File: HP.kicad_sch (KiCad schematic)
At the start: 4 parts, among them U1 BTS50010-1TAD-TBD, U2 BTS50010-1TAD-TBD, U3 BTS50010-1TAD-TBD, U4 BTS50010-1TAD-TBD

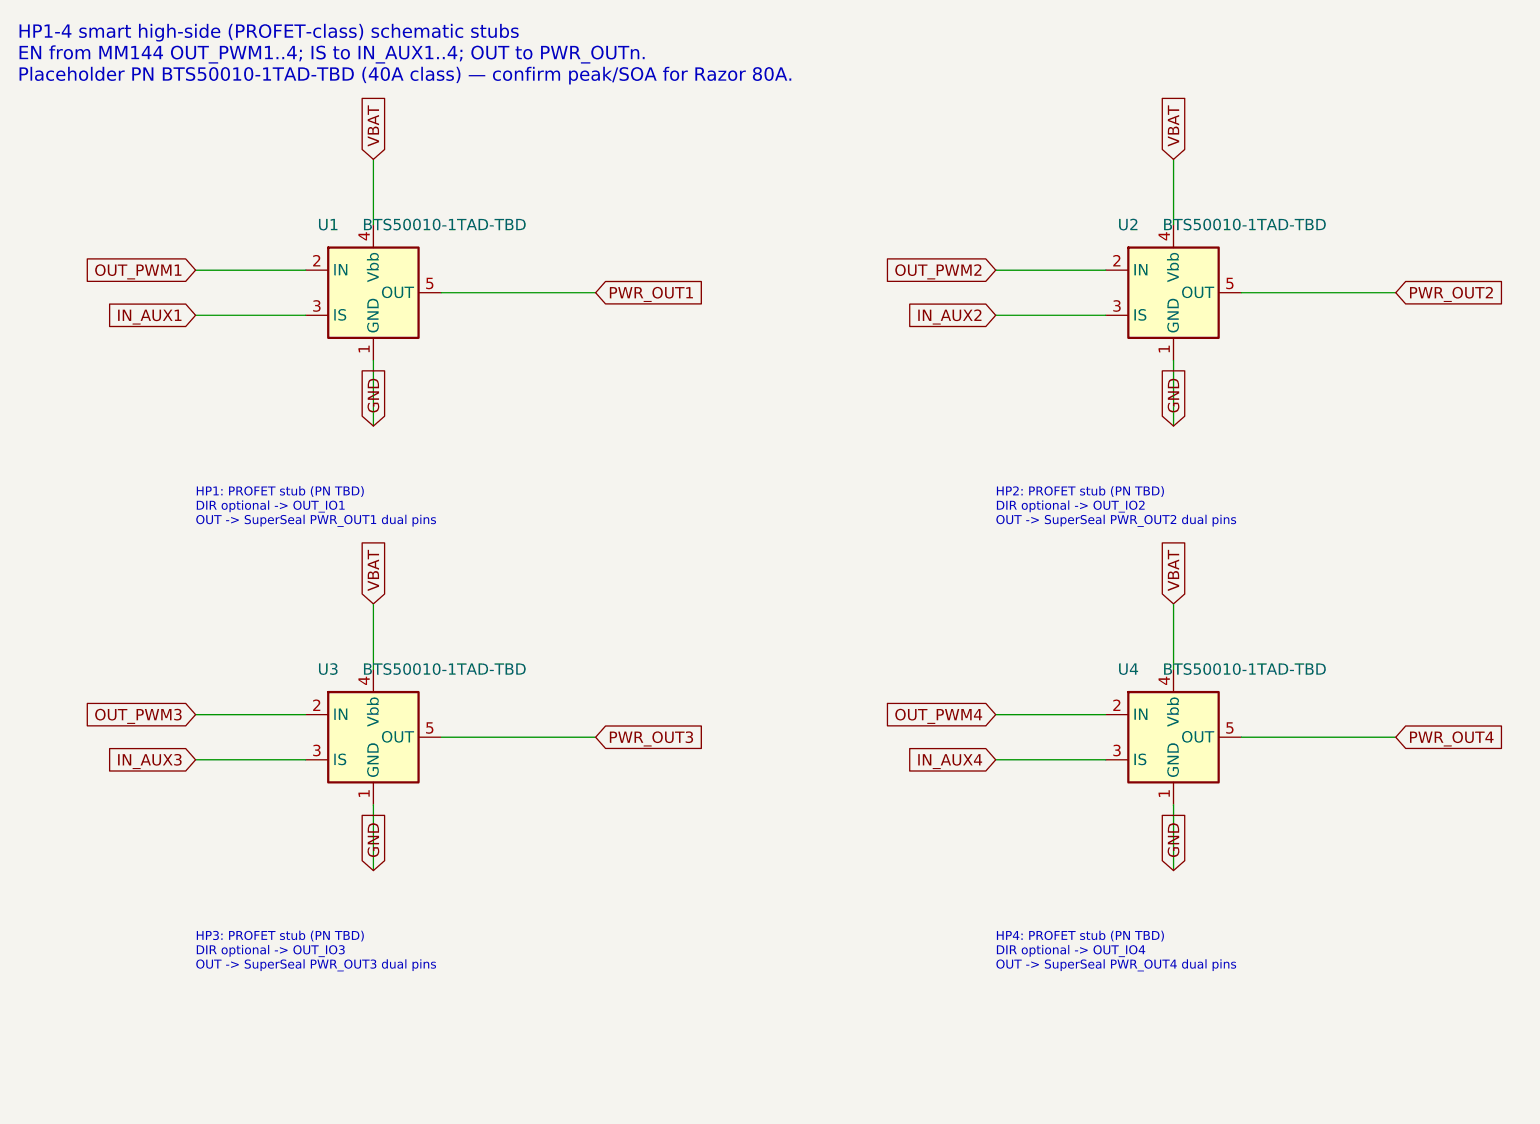
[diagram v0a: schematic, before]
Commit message: Clear fab blockers 1–4: SuperSeal 9-6437287-8, PROFET PNs, power entry, PCB place
- Replace Conn_02x13 pin-header with TE/AMP SuperSeal 1.0 26-way
  (9-6437287-8, keying 1) via pdmrazora.pretty footprint (6473423-1 pattern)
- HP: keep BTS50010-1TAD; add RIS 2k7 + 10n; fix IN/IS wiring
- ADIO: BTS7004-1EPP; RIS 4k7 + soft PU 4k7 to SENSOR_5V; fix EN/IS wiring
- Power entry: fuse/TVS/bulk stubs + IGN_SW 100k/10k (~11:1) → IN_VIGN
- PCB: place SuperSeal, HP×4, ADIO×8 with nets; outline 180×140; thermal zones
- Document PNs, kILIS, AmpsPerVolt TODOs in HARDWARE_BOM.md / BOARD.md

Do not touch HELLCORE.
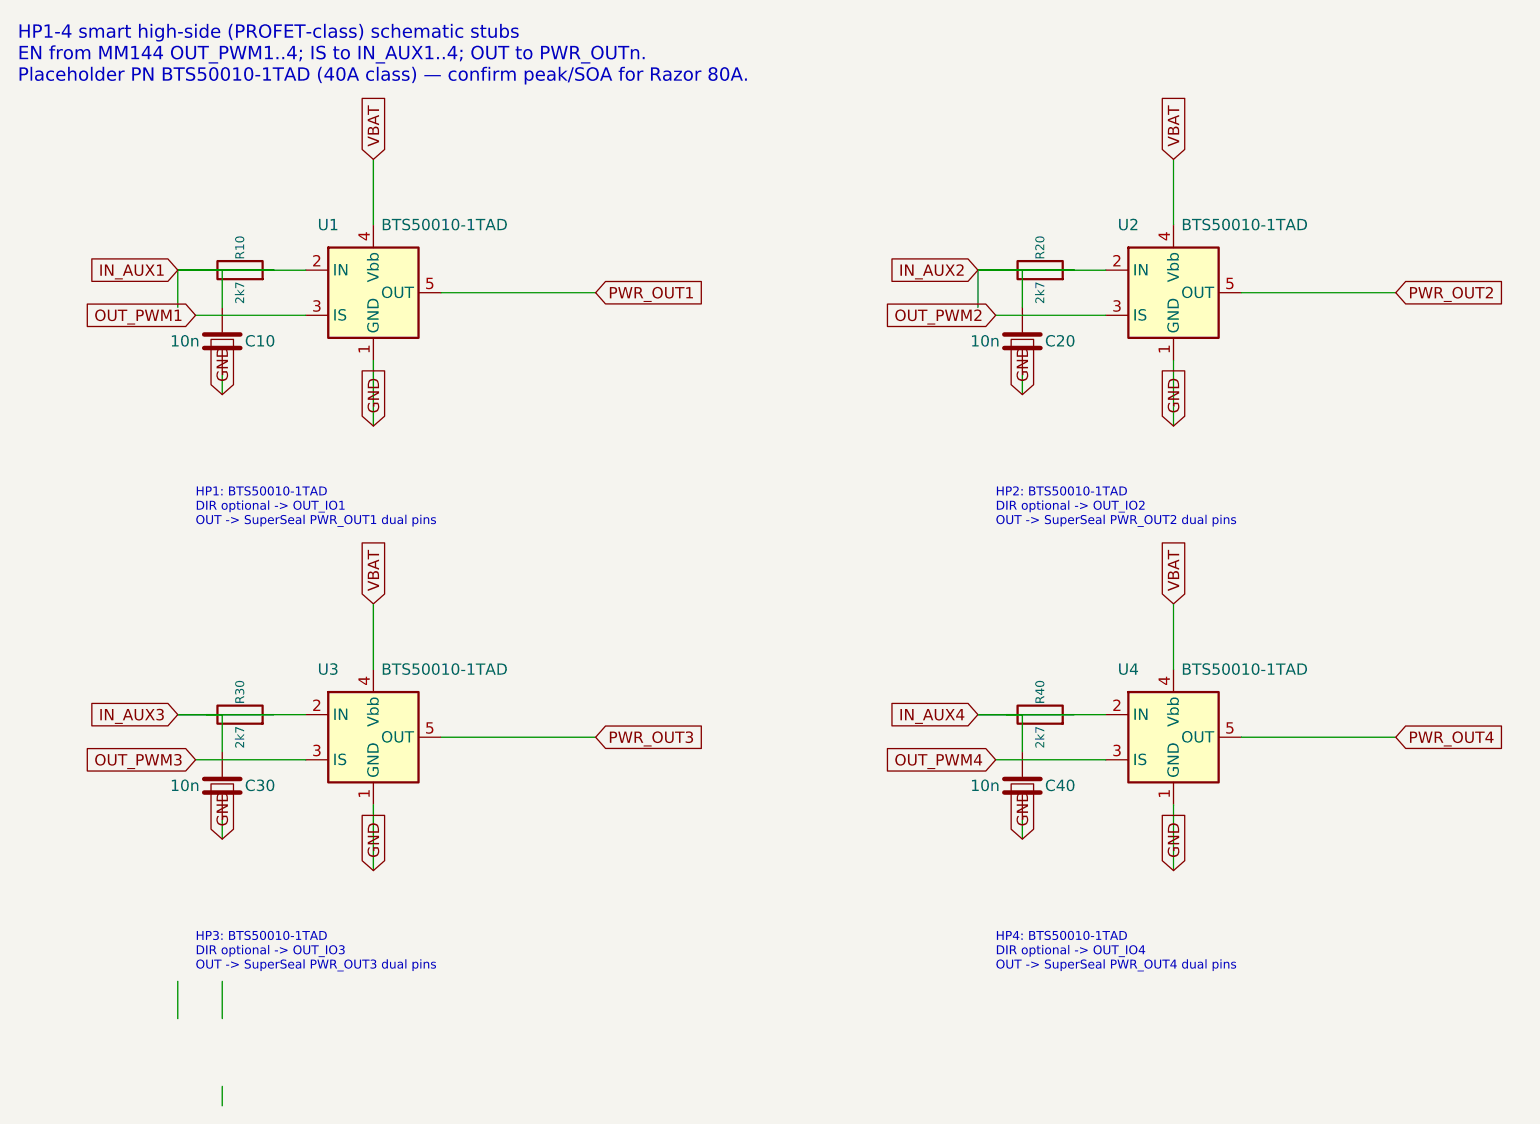
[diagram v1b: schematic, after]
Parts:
- added C10, C20, C30, C40: 10n, Capacitor_SMD:C_0603_1608Metric, symbol Device:C
- added R10, R20, R30, R40: 2k7, Resistor_SMD:R_0603_1608Metric, symbol Device:R
- U1, U2, U3, U4: value BTS50010-1TAD-TBD -> BTS50010-1TAD
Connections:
- net GND: now also C10.2, C20.2, C30.2, C40.2
- net IN_AUX1: now also U1.2 (IN), C10.1, R10.1, R10.2; no longer U1.3 (IS)
- net IN_AUX2: now also U2.2 (IN), C20.1, R20.1, R20.2; no longer U2.3 (IS)
- net IN_AUX3: now also U3.2 (IN), C30.1, R30.1, R30.2; no longer U3.3 (IS)
- net IN_AUX4: now also U4.2 (IN), C40.1, R40.1, R40.2; no longer U4.3 (IS)
- net OUT_PWM1: now also U1.3 (IS); no longer U1.2 (IN)
- net OUT_PWM2: now also U2.3 (IS); no longer U2.2 (IN)
- net OUT_PWM3: now also U3.3 (IS); no longer U3.2 (IN)
- net OUT_PWM4: now also U4.3 (IS); no longer U4.2 (IN)
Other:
- note added: "HP1-4 smart high-side (PROFET-class) schematic stubs EN from MM144 OUT_PWM1..4; IS to IN_AUX1..4; OUT to PWR_OUTn. Placeholder PN BTS50010-1TAD (40A class) — confirm peak/SOA for Razor 80A."
- note added: "HP1: BTS50010-1TAD DIR optional -> OUT_IO1 OUT -> SuperSeal PWR_OUT1 dual pins"
- note added: "HP2: BTS50010-1TAD DIR optional -> OUT_IO2 OUT -> SuperSeal PWR_OUT2 dual pins"
- note added: "HP3: BTS50010-1TAD DIR optional -> OUT_IO3 OUT -> SuperSeal PWR_OUT3 dual pins"
- note added: "HP4: BTS50010-1TAD DIR optional -> OUT_IO4 OUT -> SuperSeal PWR_OUT4 dual pins"
- note removed: "HP1-4 smart high-side (PROFET-class) schematic stubs EN from MM144 OUT_PWM1..4; IS to IN_AUX1..4; OUT to PWR_OUTn. Placeholder PN BTS50010-1TAD-TBD (40A class) — confirm peak/SOA for Razor 80A."
- note removed: "HP1: PROFET stub (PN TBD) DIR optional -> OUT_IO1 OUT -> SuperSeal PWR_OUT1 dual pins"
- note removed: "HP2: PROFET stub (PN TBD) DIR optional -> OUT_IO2 OUT -> SuperSeal PWR_OUT2 dual pins"
- note removed: "HP3: PROFET stub (PN TBD) DIR optional -> OUT_IO3 OUT -> SuperSeal PWR_OUT3 dual pins"
- note removed: "HP4: PROFET stub (PN TBD) DIR optional -> OUT_IO4 OUT -> SuperSeal PWR_OUT4 dual pins"
